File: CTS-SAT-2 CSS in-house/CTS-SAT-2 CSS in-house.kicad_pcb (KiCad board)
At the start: 2 copper layers, 38.1 x 39.8 mm, 56 parts, among them J1 Conn_01x05_Socket, J12 Socket_1x2, J13 Socket_1x2, J18 Socket_1x2, J19 Socket_1x2, U1 POPA4383PWR, U2 POPA4383PWR, U3 ADS7128IRTET

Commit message: Small edits to schematic
Changed some photodiode errors
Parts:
- J1: footprint Connector_PinHeader_2.54mm:PinHeader_1x05_P2.54mm_Vertical -> Connector_PinHeader_2.54mm:PinHeader_1x05_P2.54mm_Vertical_SMD_Pin1Left
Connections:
- LED2 pad 2: GND -> /3V3_SUPPLY_1
- LED3 pad 2: GND -> /3V3_SUPPLY_1
- LED4 pad 2: GND -> /3V3_SUPPLY_1
- LED5 pad 2: GND -> /3V3_SUPPLY_1
- LED6 pad 2: GND -> /3V3_SUPPLY_1
- LED7 pad 2: GND -> /3V3_SUPPLY_1
- LED8 pad 2: GND -> /3V3_SUPPLY_1
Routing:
- net GND: track 33.2 -> 8.68 mm, vias 20 -> 15
- net /3V3_SUPPLY_1: track 104.1 -> 128.7 mm, vias 4 -> 9

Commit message: Final schematic
Schematic is fully finished
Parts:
- added C17: 100 uF, Capacitor_SMD:C_0603_1608Metric_Pad1.08x0.95mm_HandSolder, F.Cu at (142.4, 96.5)
- added C18: 22 uF, Capacitor_SMD:C_0603_1608Metric_Pad1.08x0.95mm_HandSolder, F.Cu at (163.0, 96.2)
- added C23: 100 nF, Capacitor_SMD:C_0603_1608Metric_Pad1.08x0.95mm_HandSolder, F.Cu at (143.9, 123.2)
- added C24: 100 nF, Capacitor_SMD:C_0603_1608Metric_Pad1.08x0.95mm_HandSolder, F.Cu at (130.6, 91.7)
- added C25: 10 uF, Capacitor_SMD:C_0603_1608Metric_Pad1.08x0.95mm_HandSolder, F.Cu at (130.6, 94.3)
- added C26: 10 uF, Capacitor_SMD:C_0603_1608Metric_Pad1.08x0.95mm_HandSolder, F.Cu at (151.7, 90.8)
- added C27: 100 nF, Capacitor_SMD:C_0603_1608Metric_Pad1.08x0.95mm_HandSolder, F.Cu at (151.7, 89.3)
- added R17: 10 Ω, Capacitor_SMD:C_0603_1608Metric_Pad1.08x0.95mm_HandSolder, F.Cu at (130.3, 96.6)
- added R18: 10 Ω, Capacitor_SMD:C_0603_1608Metric_Pad1.08x0.95mm_HandSolder, F.Cu at (151.7, 92.3)
- C10, C11, C12, C2, C3, C4, C5, C6: value 32 nF -> 33 nF
- R2, R3, R4, R5, R6, R7, R8, R9: value 1.01 MΩ -> 3.3 kΩ; footprint Resistor_SMD:R_0805_2012Metric_Pad1.20x1.40mm_HandSolder -> Resistor_SMD:R_0603_1608Metric_Pad0.98x0.95mm_HandSolder
- R20, R23: footprint Resistor_SMD:R_0402_1005Metric_Pad0.72x0.64mm_HandSolder -> Resistor_SMD:R_0603_1608Metric_Pad0.98x0.95mm_HandSolder
- moved C22 56.3 mm to (140.8, 123.6)
- moved J1 25.9 mm to (143.8, 129.0)
- moved J13 16.7 mm to (141.8, 108.1)
- moved C4 16.5 mm to (147.6, 102.9)
- moved J12 16.5 mm to (148.2, 108.1)
- moved R4 13.7 mm to (147.7, 101.0)
- moved R20 8.55 mm to (144.3, 96.5)
- moved R22 8.02 mm to (134.0, 104.9)
- moved C20 7.92 mm to (127.3, 110.8)
- moved R24 7.92 mm to (135.7, 102.9)
- moved C19 7.92 mm to (127.3, 112.4)
- moved C9 7.92 mm to (124.9, 102.8)
- moved R1 7.92 mm to (131.9, 106.0)
- moved J18 7.92 mm to (125.6, 106.8)
- moved J19 7.92 mm to (119.3, 106.8)
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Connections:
- C21 pad 2: /3V3_SUPPLY_1 -> /3V3_U1
- C22 pad 2: /3V3_SUPPLY_1 -> /3V3_U1
- LED1 pad 2: GND -> Net-(LED1-CATHODE)
- LED2 pad 1: /ARRAY_SIGNAL_1 -> unconnected-(LED2-ANODE-Pad1)
- LED2 pad 2: /3V3_SUPPLY_1 -> /3V3_U1
- LED3 pad 2: /3V3_SUPPLY_1 -> /3V3_U1
- LED4 pad 2: /3V3_SUPPLY_1 -> /3V3_U1
- LED5 pad 1: /ARRAY_SIGNAL_4 -> unconnected-(LED5-ANODE-Pad1)
- LED5 pad 2: /3V3_SUPPLY_1 -> /3V3_U1
- LED6 pad 2: /3V3_SUPPLY_1 -> /3V3_U1
- LED7 pad 2: /3V3_SUPPLY_1 -> /3V3_U1
- LED8 pad 2: /3V3_SUPPLY_1 -> /3V3_U1
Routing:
- net /3V3_SUPPLY_1: track 128.7 -> 0.00 mm, vias 9 -> 0
- net /1.65V_VGND_1: track 95.5 -> 0.00 mm, vias 6 -> 0
- net /TIA_OUTPUT_5: track 38.9 -> 0.00 mm, vias 2 -> 0
- net /TIA_OUPTUT_1: track 37.0 -> 0.00 mm, vias 2 -> 0
- net /TIA_OUTPUT_2: track 26.1 -> 0.00 mm, vias 2 -> 0
- net /TIA_OUTPUT_4: track 25.5 -> 0.00 mm, vias 2 -> 0
- net /TIA_OUTPUT_6: track 24.0 -> 0.00 mm, vias 2 -> 0
- net /COURSE_TIA_OUTPUT: track 23.0 -> 0.00 mm
- net Net-(J13-Pin_2): track 20.3 -> 0.00 mm
- net /TIA_OUTPUT_7: track 20.0 -> 0.00 mm
- net /ARRAY_SIGNAL_1: track 19.9 -> 0.00 mm
- net /ARRAY_SIGNAL_3: track 19.4 -> 0.00 mm
- net /ARRAY_SIGNAL_2: track 18.0 -> 0.00 mm
- net /TIA_OUTPUT_3: track 17.6 -> 0.00 mm, vias 2 -> 0
- net /ARRAY_SIGNAL_5: track 17.5 -> 0.00 mm
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- removed copper zone on B.Cu, net GND
- removed copper zone on F.Cu, net GND
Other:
- board outline removed

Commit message: Pcb designing
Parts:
- moved C22 53.1 mm to (115.6, 76.8)
- moved C18 28.0 mm to (138.5, 109.8)
- moved J12 18.7 mm to (149.1, 89.4), turned to -90 degrees
- moved J13 14.4 mm to (149.1, 95.7), turned to -90 degrees
- moved C4 12.3 mm to (145.1, 90.9), turned to 90 degrees
- moved C19 8.90 mm to (133.2, 119.0)
- moved C20 8.90 mm to (133.3, 117.4)
- moved J18 8.27 mm to (125.9, 115.1)
- moved J19 8.27 mm to (119.7, 115.1)
- moved C21 7.91 mm to (145.0, 74.5)
- moved R4 7.19 mm to (145.1, 94.3), turned to -90 degrees
- moved R20 4.86 mm to (140.7, 93.2)
- moved C17 4.63 mm to (139.1, 93.2), turned to -90 degrees
- moved R23 4.56 mm to (137.6, 93.2)
- moved C24 4.25 mm to (131.4, 95.9), turned to -90 degrees
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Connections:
- LED2 pad 1: unconnected-(LED2-ANODE-Pad1) -> /ARRAY_SIGNAL_1
- LED5 pad 1: unconnected-(LED5-ANODE-Pad1) -> /ARRAY_SIGNAL_4
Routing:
- net Net-(J13-Pin_2): track 0.00 -> 26.4 mm
- net /3V3_U1: track 0.00 -> 23.7 mm
- net /ARRAY_SIGNAL_6: track 0.00 -> 17.7 mm
- net Net-(LED1-CATHODE): track 0.00 -> 17.2 mm
- net /1.65V_VGND_1: track 0.00 -> 16.4 mm, vias 0 -> 1
- net /ARRAY_SIGNAL_5: track 0.00 -> 16.3 mm
- net /ARRAY_SIGNAL_7: track 0.00 -> 16.3 mm
- net /ARRAY_SIGNAL_4: track 0.00 -> 15.0 mm
- net /TIA_OUTPUT_5: track 0.00 -> 13.8 mm
- net /TIA_OUPTUT_1: track 0.00 -> 13.8 mm
- net /TIA_OUTPUT_7: track 0.00 -> 13.4 mm
- net /ARRAY_SIGNAL_2: track 0.00 -> 13.1 mm
- net /TIA_OUTPUT_4: track 0.00 -> 10.5 mm
- net /TIA_OUTPUT_6: track 0.00 -> 9.75 mm
- net /TIA_OUTPUT_3: track 0.00 -> 8.56 mm
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
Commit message: Final before design review
Fully finished schematic, pcb placement and pcb routing.
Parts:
- added REF**: ToolingHole_1.152mm, MountingHole:ToolingHole_1.152mm, F.Cu at (152.9, 70.7)
- added REF**: ToolingHole_1.152mm, MountingHole:ToolingHole_1.152mm, F.Cu at (115.9, 107.7)
- added REF**: ToolingHole_1.152mm, MountingHole:ToolingHole_1.152mm, F.Cu at (152.8, 107.7)
- added REF**: ToolingHole_1.152mm, MountingHole:ToolingHole_1.152mm, F.Cu at (115.9, 70.7)
- moved J1 23.5 mm to (144.3, 105.5)
- moved C23 20.7 mm to (131.4, 106.7), turned to -90 degrees
- moved J18 19.4 mm to (120.5, 96.4), turned to 90 degrees
- moved C19 14.1 mm to (126.5, 106.6), turned to -90 degrees
- moved J19 12.5 mm to (120.5, 102.7), turned to 90 degrees
- moved C20 11.9 mm to (128.1, 106.6), turned to -90 degrees
- moved R1 11.3 mm to (141.0, 101.0), turned to 0 degrees
- moved C26 9.90 mm to (150.1, 83.7)
- moved R18 9.90 mm to (150.1, 85.2)
- moved C27 9.90 mm to (150.1, 82.1)
- moved R22 9.56 mm to (141.0, 99.0), turned to 0 degrees
- moved C18 9.27 mm to (129.7, 106.7), turned to -90 degrees
- moved R24 8.57 mm to (141.0, 97.1), turned to 0 degrees
- moved C9 7.98 mm to (124.5, 97.8), turned to 90 degrees
- moved R5 4.18 mm to (135.4, 87.0), turned to 0 degrees
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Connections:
- net Net-(J13-Pin_2) renamed /CSS_ARRAY_SIGNAL
- C21 pad 1: Net-(U1-V+) -> /3V3_U1
- C21 pad 2: /3V3_U1 -> GND
- C22 pad 1: Net-(U2-V+) -> /3V3_U1
- C22 pad 2: /3V3_U1 -> GND
- U1 pad 4: Net-(U1-V+) -> /3V3_U1
- U2 pad 4: Net-(U2-V+) -> /3V3_U1
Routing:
- net /3V3_SUPPLY_1: track 0.36 -> 85.8 mm, vias 0 -> 6
- net /3V3_U1: track 23.7 -> 89.1 mm
- net /1.65V_VGND_1: track 16.4 -> 63.2 mm, vias 1 -> 2
- net /TIA_OUPTUT_1: track 13.8 -> 47.7 mm, vias 0 -> 2
- net /COURSE_TIA_OUTPUT: track 6.76 -> 36.8 mm, vias 0 -> 2
- net /TIA_OUTPUT_5: track 13.8 -> 43.5 mm, vias 0 -> 2
- net /TIA_OUTPUT_4: track 10.5 -> 33.5 mm, vias 0 -> 2
- net Net-(J1-Pin_1): track 0.00 -> 20.7 mm
- net GND: track 7.31 -> 27.3 mm, vias 1 -> 73
- net Net-(J1-Pin_2): track 0.00 -> 20.0 mm
- net /TIA_OUTPUT_2: track 7.17 -> 27.0 mm, vias 0 -> 2
- net /TIA_OUTPUT_6: track 9.75 -> 29.3 mm, vias 0 -> 2
- net Net-(J18-Pin_1): track 0.00 -> 18.6 mm, vias 0 -> 2
- net /TIA_OUTPUT_3: track 8.56 -> 23.7 mm, vias 0 -> 2
- net Net-(J1-Pin_3): track 0.00 -> 13.9 mm
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- added copper zone on B.Cu, net GND
- added copper zone on F.Cu, net GND
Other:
- board outline added: 40 x 40 mm
- board text added: "{ "ViaStitcher": "0.3.1", "stitch_zone_0": { "HSpacing": "2.5", "VSpacing": "2.5", "HOffset": "0", "VOffset": "0", "Clearance": "0.5", "Randomize": false, "Stagger": false, "OnlyFilledCopper": true } }"

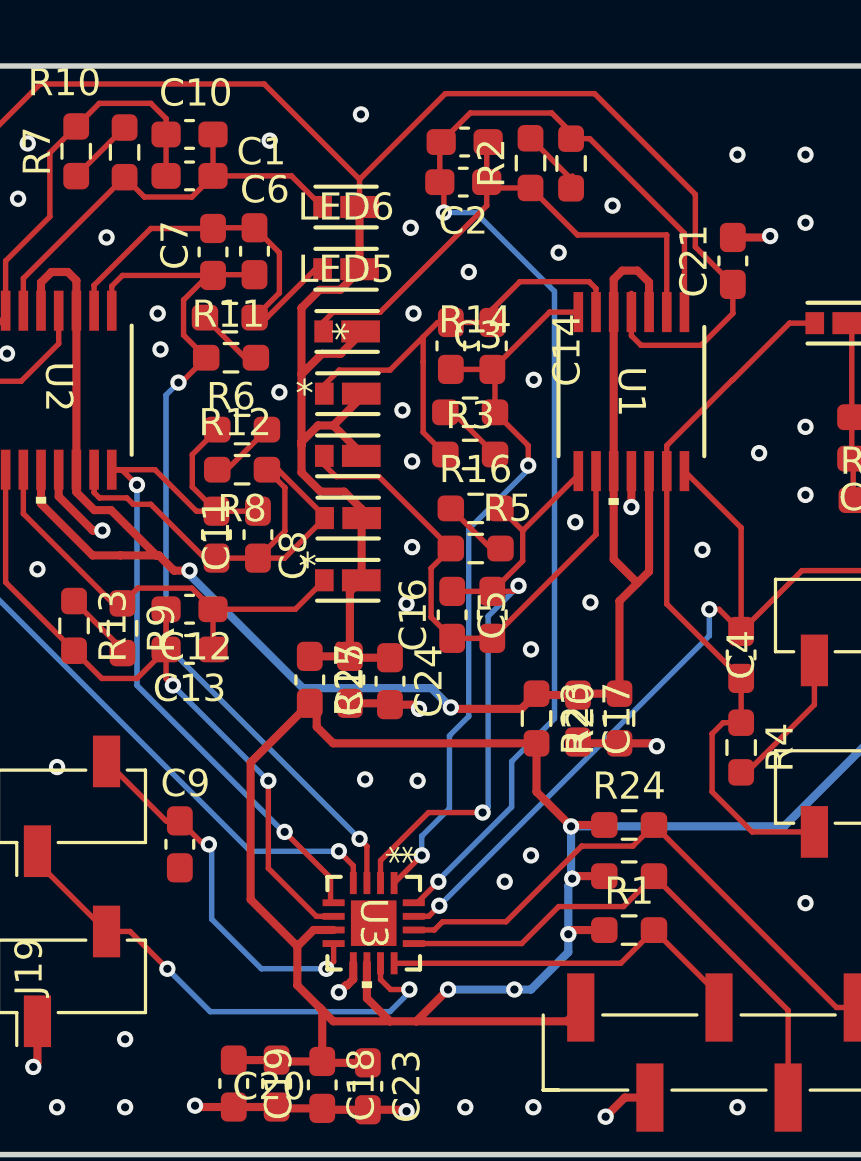
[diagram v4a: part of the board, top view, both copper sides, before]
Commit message: Fixed a ground plane issue
fixed a drc issue i missed
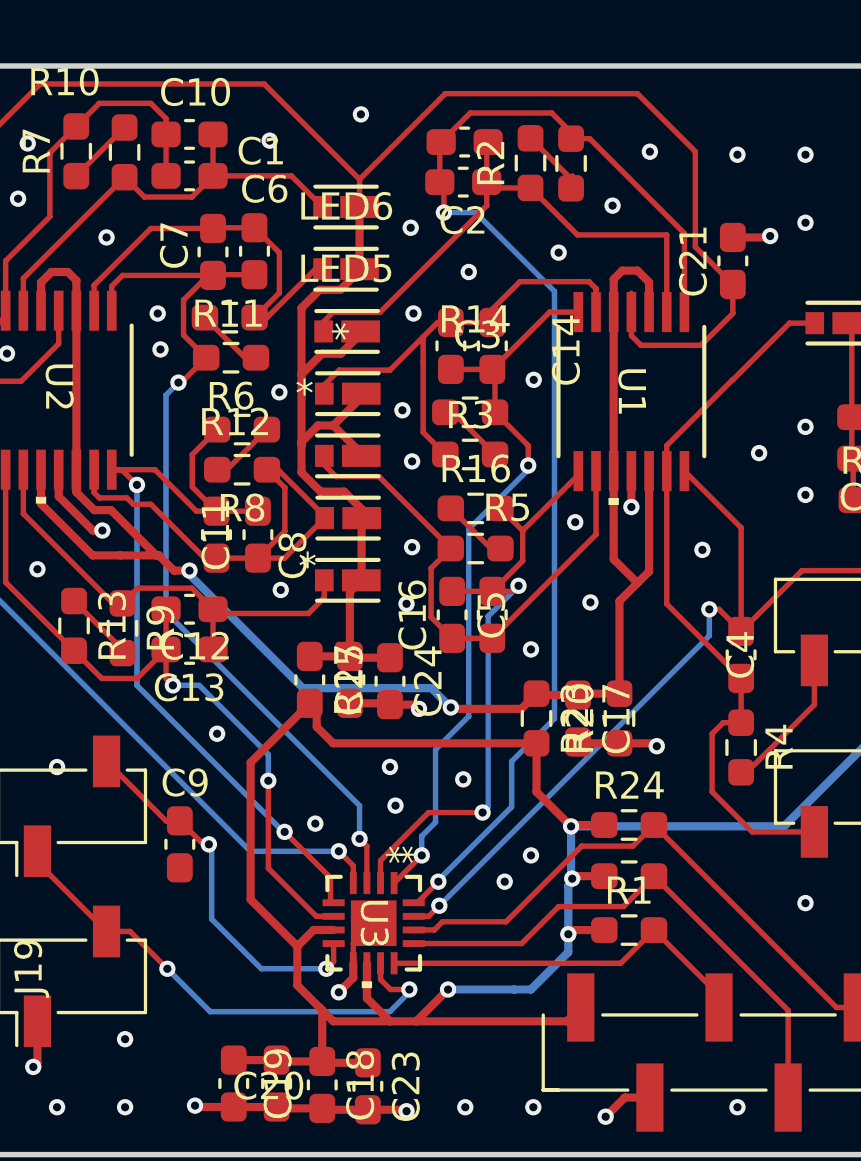
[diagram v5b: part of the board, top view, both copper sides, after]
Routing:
- net GND: track 27.3 -> 29.1 mm, vias 73 -> 78
- net /3V3_U1: track 89.1 -> 90.0 mm
- net /TIA_OUTPUT_7: track 26.1 -> 26.7 mm
- net /ARRAY_SIGNAL_7: track 16.5 -> 17.0 mm
- net /3V3_SUPPLY_1: vias 6 -> 5
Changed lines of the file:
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@@
-	)
-	(via
-		(at 136.8044 103.1748)
-		(size 0.6)
-		(drill 0.3)
-		(layers "F.Cu" "B.Cu")
-		(net "/3V3_SUPPLY_1")
 	)
 	(via
@@
 	)
 	(segment
-		(start 130.6576 103.0224)
-		(end 130.884798 102.795202)
-		(width 0.3)
-		(layer "F.Cu")
-		(net "GND")
-	)
-	(segment
-		(start 130.884798 102.795202)
-		(end 130.884798 102.2096)
+		(start 130.884798 102.2096)
+		(end 130.884798 102.744402)
 		(width 0.3)
 		(layer "F.Cu")
@@
 	)
 	(segment
-		(start 130.3528 103.2764)
-		(end 130.6068 103.0224)
+		(start 130.884798 102.744402)
+		(end 130.3528 103.2764)
 		(width 0.3)
 		(layer "F.Cu")
@@
 	)
 	(segment
-		(start 130.6068 103.0224)
-		(end 130.6576 103.0224)
-		(width 0.3)
-		(layer "F.Cu")
-		(net "GND")
-	)
-	(segment
 		(start 132.2324 92.7078)
 		(end 133.1446 92.7078)
@@
 	)
 	(segment
+		(start 130.884798 102.2096)
+		(end 130.884798 101.486401)
+		(width 0.2)
+		(layer "F.Cu")
+		(net "GND")
+	)
+	(segment
 		(start 121.3104 86.3092)
 		(end 121.666 86.3092)
@@
 	)
 	(segment
+		(start 130.884798 101.486401)
+		(end 131.634799 100.7364)
+		(width 0.2)
+		(layer "F.Cu")
+		(net "GND")
+	)
+	(segment
 		(start 116.1288 74.422)
 		(end 115.9764 74.2696)
@@
 	)
 	(via
+		(at 125.8824 93.7768)
+		(size 0.6)
+		(drill 0.3)
+		(layers "F.Cu" "B.Cu")
+		(free yes)
+		(net "GND")
+	)
+	(via
 		(at 140.1572 107.8484)
 		(size 0.6)
@@
 	)
 	(via
+		(at 129.4892 97.0788)
+		(size 0.6)
+		(drill 0.3)
+		(layers "F.Cu" "B.Cu")
+		(free yes)
+		(net "GND")
+	)
+	(via
 		(at 117.5 100)
 		(size 0.6)
@@
 	)
 	(via
-		(at 133.2484 95.504)
+		(at 141.7828 72.39)
+		(size 0.6)
+		(drill 0.3)
+		(layers "F.Cu" "B.Cu")
+		(free yes)
+		(net "GND")
+	)
+	(via
+		(at 132.4356 96.4184)
 		(size 0.6)
 		(drill 0.3)
@@
 	)
 	(via
-		(at 131.318 95.4532)
+		(at 132.2324 94.996)
 		(size 0.6)
 		(drill 0.3)
@@
 	)
 	(via
+		(at 134.9248 95.4532)
+		(size 0.6)
+		(drill 0.3)
+		(layers "F.Cu" "B.Cu")
+		(free yes)
+		(net "GND")
+	)
+	(via
 		(at 147.5 75)
 		(size 0.6)
@@
 	(via
 		(at 122.5 105)
+		(size 0.6)
+		(drill 0.3)
+		(layers "F.Cu" "B.Cu")
+		(free yes)
+		(net "GND")
+	)
+	(via
+		(at 128.2192 88.4936)
 		(size 0.6)
 		(drill 0.3)
@@
 	)
 	(segment
-		(start 131.1148 97.6376)
-		(end 124.0028 90.5256)
-		(width 0.2)
-		(layer "B.Cu")
-		(net "/TIA_OUTPUT_4")
-	)
-	(segment
 		(start 124.0028 81.3308)
 		(end 124.46 80.8736)
@@
 	)
 	(segment
-		(start 124.0028 90.5256)
+		(start 131.1148 97.6376)
+		(end 131.1148 96.4184)
+		(width 0.2)
+		(layer "B.Cu")
+		(net "/TIA_OUTPUT_4")
+	)
+	(segment
+		(start 124.0028 89.3064)
 		(end 124.0028 81.3308)
+		(width 0.2)
+		(layer "B.Cu")
+		(net "/TIA_OUTPUT_4")
+	)
+	(segment
+		(start 131.1148 96.4184)
+		(end 124.0028 89.3064)
 		(width 0.2)
 		(layer "B.Cu")
@@
 	)
 	(segment
+		(start 134.2644 70.2564)
+		(end 131.1148 73.406)
+		(width 0.2)
+		(layer "F.Cu")
+		(net "/3V3_U1")
+	)
+	(segment
+		(start 143.4528 72.3836)
+		(end 141.3256 70.2564)
+		(width 0.2)
+		(layer "F.Cu")
+		(net "/3V3_U1")
+	)
+	(segment
 		(start 131.1148 78.9559)
 		(end 131.1529 78.994)
@@
 	)
 	(segment
-		(start 143.4528 75.8877)
-		(end 143.4528 73.9584)
-		(width 0.2)
-		(layer "F.Cu")
-		(net "/3V3_U1")
-	)
-	(segment
-		(start 139.7508 70.2564)
-		(end 134.2644 70.2564)
-		(width 0.2)
-		(layer "F.Cu")
-		(net "/3V3_U1")
-	)
-	(segment
 		(start 129.6837 84.8796)
 		(end 128.9812 84.1771)
@@
 	)
 	(segment
+		(start 141.3256 70.2564)
+		(end 134.2644 70.2564)
+		(width 0.2)
+		(layer "F.Cu")
+		(net "/3V3_U1")
+	)
+	(segment
 		(start 130.5488 84.8796)
 		(end 129.6837 84.8796)
@@
 	)
 	(segment
+		(start 143.4528 75.8877)
+		(end 143.4528 72.3836)
+		(width 0.2)
+		(layer "F.Cu")
+		(net "/3V3_U1")
+	)
+	(segment
 		(start 130.7592 88.5571)
 		(end 131.1783 88.138)
@@
 	)
 	(segment
-		(start 134.2644 70.2564)
-		(end 131.1148 73.406)
-		(width 0.2)
-		(layer "F.Cu")
-		(net "/3V3_U1")
-	)
-	(segment
 		(start 141.102799 79.147201)
 		(end 141.457598 79.502)
@@
 	)
 	(segment
+		(start 144.8308 77.2657)
+		(end 143.4528 75.8877)
+		(width 0.2)
+		(layer "F.Cu")
+		(net "/3V3_U1")
+	)
+	(segment
 		(start 128.9812 78.1304)
 		(end 129.6472 77.4644)
@@
 	)
 	(segment
-		(start 143.4528 73.9584)
-		(end 139.7508 70.2564)
-		(width 0.2)
-		(layer "F.Cu")
-		(net "/3V3_U1")
-	)
-	(segment
 		(start 130.4092 77.4644)
 		(end 131.1148 76.7588)
@@
 	)
 	(segment
-		(start 144.8308 77.2657)
-		(end 143.4528 75.8877)
-		(width 0.2)
-		(layer "F.Cu")
-		(net "/3V3_U1")
-	)
-	(segment
 		(start 131.1783 83.566)
 		(end 131.1783 83.4756)
@@
 	)
 	(segment
+		(start 127.762 94.5388)
+		(end 125.222 91.9988)
+		(width 0.2)
+		(layer "B.Cu")
+		(net "/TIA_OUTPUT_7")
+	)
+	(segment
+		(start 125.222 91.9988)
+		(end 124.2568 91.9988)
+		(width 0.2)
+		(layer "B.Cu")
+		(net "/TIA_OUTPUT_7")
+	)
+	(segment
 		(start 127.762 95.504)
-		(end 124.2568 91.9988)
+		(end 127.762 94.5388)
 		(width 0.2)
 		(layer "B.Cu")
 		(net "/TIA_OUTPUT_7")
-	)
-	(segment
-		(start 129.8194 88.138)
-		(end 128.7559 89.2015)
-		(width 0.2)
-		(layer "F.Cu")
-		(net "/ARRAY_SIGNAL_7")
 	)
 	(segment
@@
 	)
 	(segment
+		(start 129.8194 88.138)
+		(end 129.8194 88.773)
+		(width 0.2)
+		(layer "F.Cu")
+		(net "/ARRAY_SIGNAL_7")
+	)
+	(segment
 		(start 122.4015 88.9875)
 		(end 122.9625 88.4265)
@@
 	)
 	(segment
+		(start 125.8857 89.3572)
+		(end 125.73 89.2015)
+		(width 0.2)
+		(layer "F.Cu")
+		(net "/ARRAY_SIGNAL_7")
+	)
+	(segment
+		(start 129.8194 88.773)
+		(end 129.2352 89.3572)
+		(width 0.2)
+		(layer "F.Cu")
+		(net "/ARRAY_SIGNAL_7")
+	)
+	(segment
 		(start 125.73 90.678)
 		(end 125.73 89.2015)
@@
 	)
 	(segment
-		(start 128.7559 89.2015)
-		(end 125.73 89.2015)
+		(start 129.2352 89.3572)
+		(end 125.8857 89.3572)
 		(width 0.2)
 		(layer "F.Cu")
@@
 	)
 	(segment
-		(start 134.4168 96.52)
-		(end 134.4168 93.852271)
+		(start 133.4008 98.2472)
+		(end 133.4008 97.536)
 		(width 0.2)
 		(layer "B.Cu")
@@
 	)
 	(segment
+		(start 133.9088 97.028)
+		(end 133.9088 94.360271)
+		(width 0.2)
+		(layer "B.Cu")
+		(net "/TIA_OUTPUT_2")
+	)
+	(segment
 		(start 133.4008 97.536)
-		(end 134.4168 96.52)
+		(end 133.9088 97.028)
 		(width 0.2)
 		(layer "B.Cu")
@@
 	)
 	(segment
-		(start 134.4168 93.852271)
-		(end 135.128 93.141071)
-		(width 0.2)
-		(layer "B.Cu")
-		(net "/TIA_OUTPUT_2")
-	)
-	(segment
 		(start 135.128 93.141071)
 		(end 135.128 86.2584)
@@
 	)
 	(segment
-		(start 133.4008 98.2472)
-		(end 133.4008 97.536)
-		(width 0.2)
-		(layer "B.Cu")
+		(start 133.9088 94.360271)
+		(end 135.128 93.141071)
+		(width 0.2)
+		(layer "B.Cu")
